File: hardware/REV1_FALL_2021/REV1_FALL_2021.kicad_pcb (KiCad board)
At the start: 2 copper layers, 146 x 133.4 mm, 40 parts, among them J101 Screw_Terminal_01x02, J102 Screw_Terminal_01x02, Q101 Q_NMOS_GDS, Q102 Q_NMOS_GDS, U1 Teensy3.6_All_Pins, U2 PA16165_Breakout, U201 TPS2113ADRBR, U3 MPL3115A2_Breakout, U301 TPS2113ADRBR, U4 BNO055_Breakout, U5 RFM69HCW_Breakout

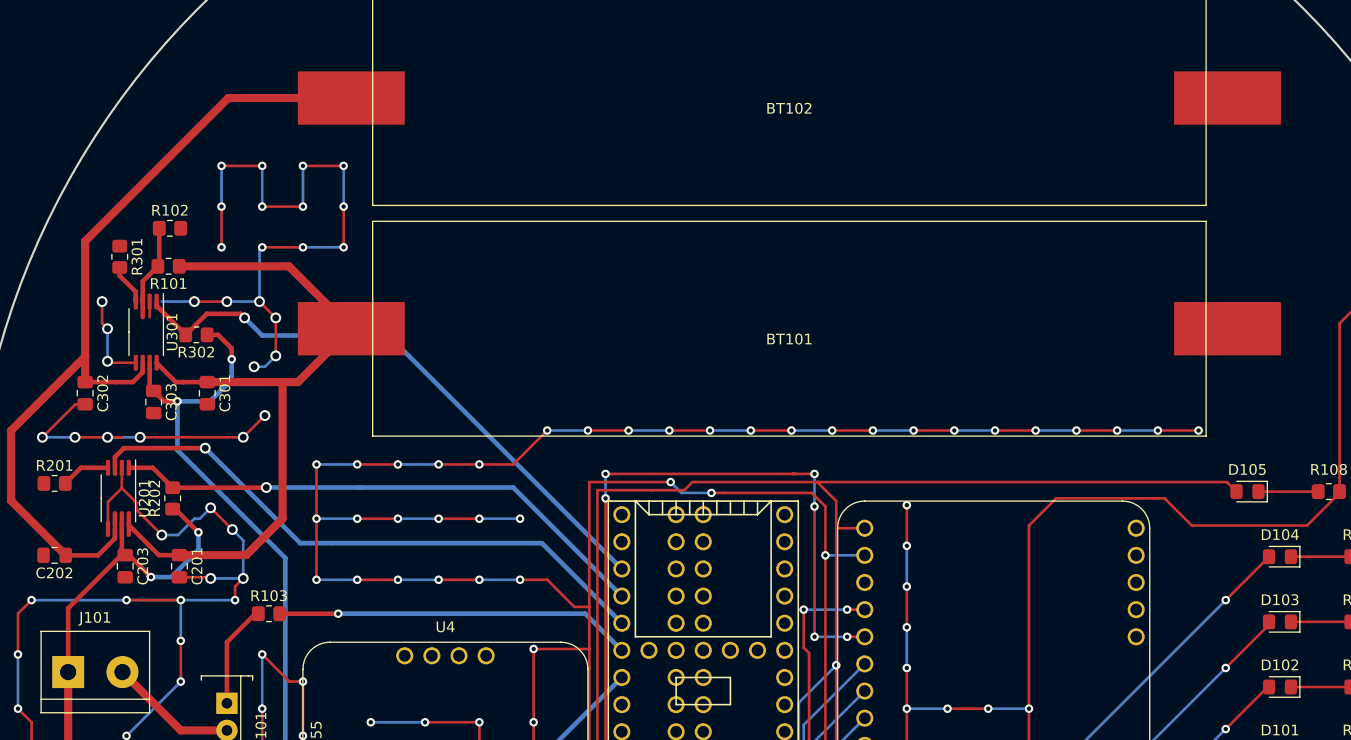
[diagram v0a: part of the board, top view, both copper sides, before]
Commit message: add dot to pin 1 of TPS2113A, rewire traces slightly
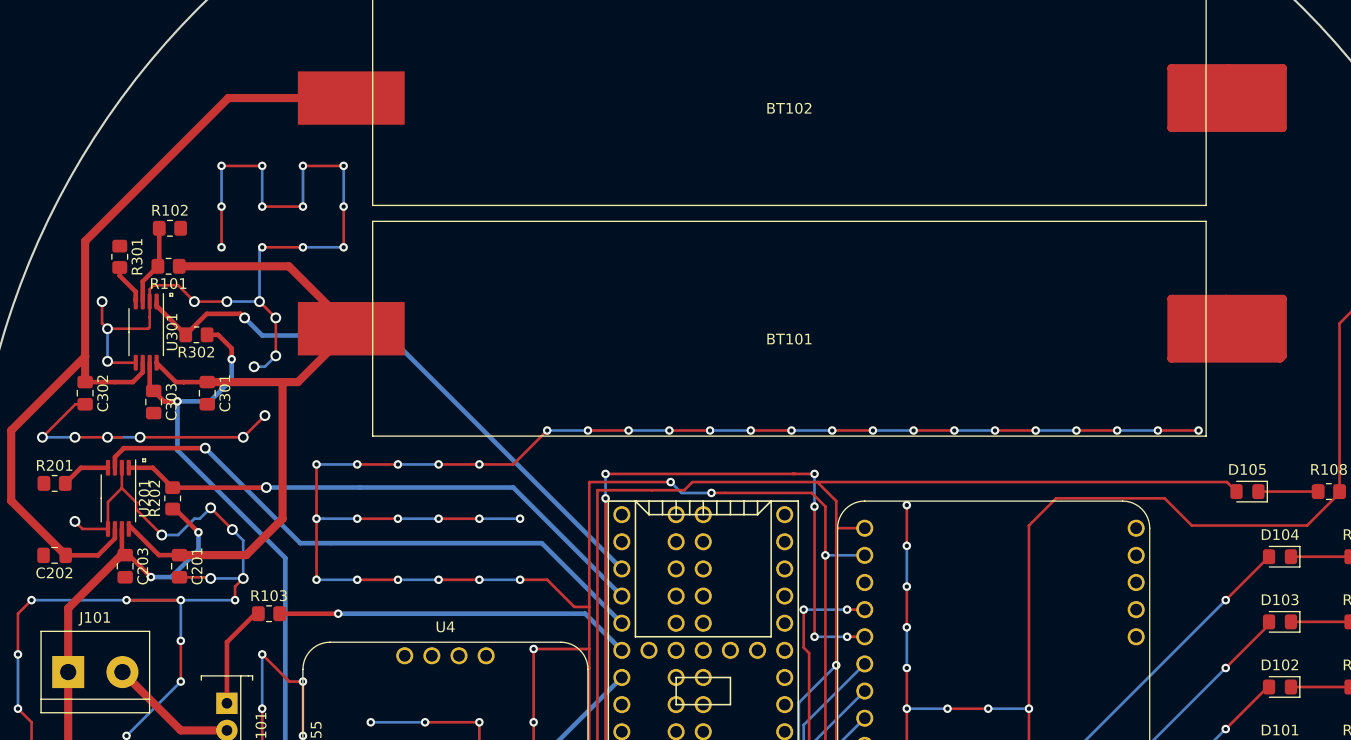
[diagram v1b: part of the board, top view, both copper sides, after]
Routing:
- net GND: track 996.9 -> 1075.0 mm, vias 176 -> 177
- net /V_EMATCH: track 63.3 -> 75.0 mm
- net /TPS2113A for Teensy power/VSNS: track 9.31 -> 7.49 mm
- net /TPS2113A for E-match/IN1: track 70.6 -> 69.5 mm
- net /TPS2113A for E-match/IN2: track 82.5 -> 81.4 mm
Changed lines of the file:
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@@
   (general
     (thickness 1.6)
-    (drawings 8)
-    (tracks 693)
+    (drawings 16)
+    (tracks 714)
     (zones 0)
     (modules 40)
@@
   )
   (setup
-    (last_trace_width 0.4318)
+    (last_trace_width 0.762)
     (user_trace_width 0.4318)
     (user_trace_width 0.762)
@@
     )
   )
+  (gr_line (start 43.688 93.726) (end 43.434 93.726) (angle 90) (layer F.SilkS) (width 0.12))
+  (gr_line (start 43.688 93.472) (end 43.688 93.726) (angle 90) (layer F.SilkS) (width 0.12))
+  (gr_line (start 43.434 93.472) (end 43.688 93.472) (angle 90) (layer F.SilkS) (width 0.12))
+  (gr_line (start 43.434 93.726) (end 43.434 93.472) (angle 90) (layer F.SilkS) (width 0.12))
+  (gr_line (start 46.228 77.978) (end 46.228 78.232) (angle 90) (layer F.SilkS) (width 0.12))
+  (gr_line (start 45.974 77.978) (end 46.228 77.978) (angle 90) (layer F.SilkS) (width 0.12))
+  (gr_line (start 45.974 78.232) (end 45.974 77.978) (angle 90) (layer F.SilkS) (width 0.12))
+  (gr_line (start 46.228 78.232) (end 45.974 78.232) (angle 90) (layer F.SilkS) (width 0.12))
   (gr_text - (at 134.62 45.72) (layer F.SilkS)
     (effects (font (size 3.81 3.81) (thickness 0.3)))
@@
   (segment (start 40.132 84.328) (end 40.132 81.28) (width 0.25) (layer B.Cu) (net 12))
   (via (at 40.132 84.328) (size 1.016) (drill 0.635) (layers F.Cu B.Cu) (net 12))
-  (segment (start 44.0765 80.1975) (end 44.0765 79.3675) (width 0.25) (layer F.Cu) (net 12) (status 400020))
+  (segment (start 44.0765 79.3675) (end 44.0765 80.1975) (width 0.25) (layer F.Cu) (net 12) (status 800020))
+  (segment (start 43.942 81.28) (end 40.132 81.28) (width 0.25) (layer F.Cu) (net 12))
+  (segment (start 44.0765 81.1455) (end 43.942 81.28) (width 0.25) (layer F.Cu) (net 12))
+  (segment (start 44.0765 80.1975) (end 44.0765 81.1455) (width 0.25) (layer F.Cu) (net 12))
   (via (at 53.848 84.836) (size 1.016) (drill 0.635) (layers F.Cu B.Cu) (net 12))
   (segment (start 54.864 84.836) (end 53.848 84.836) (width 0.25) (layer B.Cu) (net 12))
@@
   (via (at 55.88 83.82) (size 1.016) (drill 0.635) (layers F.Cu B.Cu) (net 12))
   (segment (start 55.88 80.264) (end 55.88 83.82) (width 0.25) (layer F.Cu) (net 12))
-  (segment (start 45.212 78.74) (end 48.26 78.74) (width 0.25) (layer B.Cu) (net 12))
   (via (at 48.26 78.74) (size 1.016) (drill 0.635) (layers F.Cu B.Cu) (net 12))
+  (segment (start 46.736 77.216) (end 48.26 78.74) (width 0.25) (layer F.Cu) (net 12))
+  (segment (start 44.45 77.216) (end 46.736 77.216) (width 0.25) (layer F.Cu) (net 12))
+  (segment (start 44.0765 77.5895) (end 44.45 77.216) (width 0.25) (layer F.Cu) (net 12))
+  (segment (start 44.0765 78.735) (end 44.0765 77.5895) (width 0.25) (layer F.Cu) (net 12) (status 400000))
+  (segment (start 51.308 78.74) (end 54.356 78.74) (width 0.25) (layer B.Cu) (net 12))
+  (via (at 51.308 78.74) (size 1.016) (drill 0.635) (layers F.Cu B.Cu) (net 12))
   (segment (start 48.26 78.74) (end 51.308 78.74) (width 0.25) (layer F.Cu) (net 12))
-  (via (at 51.308 78.74) (size 1.016) (drill 0.635) (layers F.Cu B.Cu) (net 12))
-  (segment (start 51.308 78.74) (end 54.356 78.74) (width 0.25) (layer B.Cu) (net 12))
   (via (at 54.356 78.74) (size 1.016) (drill 0.635) (layers F.Cu B.Cu) (net 12))
   (segment (start 54.356 78.74) (end 55.88 80.264) (width 0.25) (layer F.Cu) (net 12))
@@
   (segment (start 40.173 100.0175) (end 40.173 97.495) (width 0.25) (layer F.Cu) (net 12) (status 400000))
   (segment (start 40.173 97.495) (end 41.473 96.195) (width 0.25) (layer F.Cu) (net 12))
-  (segment (start 41.473 98.555) (end 41.473 101.854) (width 0.4318) (layer F.Cu) (net 13) (status 400000))
-  (segment (start 41.473 101.854) (end 41.473 102.1575) (width 0.4318) (layer F.Cu) (net 13) (status 800020))
+  (segment (start 145.034 56.896) (end 139.7 56.896) (width 0.762) (layer F.Cu) (net 12))
+  (segment (start 150.114 56.896) (end 145.034 56.896) (width 0.762) (layer F.Cu) (net 12))
+  (segment (start 150.114 62.484) (end 150.114 56.896) (width 0.762) (layer F.Cu) (net 12))
+  (segment (start 139.7 62.484) (end 150.114 62.484) (width 0.762) (layer F.Cu) (net 12))
+  (segment (start 139.7 56.896) (end 139.7 62.484) (width 0.762) (layer F.Cu) (net 12))
+  (segment (start 144.945 81.28) (end 144.945 78.575) (width 0.762) (layer F.Cu) (net 12) (status 400000))
+  (segment (start 150.114 78.486) (end 144.78 78.486) (width 0.762) (layer F.Cu) (net 12))
+  (segment (start 150.114 83.82) (end 150.114 78.486) (width 0.762) (layer F.Cu) (net 12))
+  (segment (start 139.7 78.486) (end 139.7 84.074) (width 0.762) (layer F.Cu) (net 12))
+  (segment (start 144.856 78.486) (end 139.7 78.486) (width 0.762) (layer F.Cu) (net 12))
+  (segment (start 144.945 78.575) (end 144.856 78.486) (width 0.762) (layer F.Cu) (net 12))
+  (segment (start 139.7 84.074) (end 149.86 84.074) (width 0.762) (layer F.Cu) (net 12))
+  (segment (start 149.86 84.074) (end 150.114 83.82) (width 0.762) (layer F.Cu) (net 12))
+  (segment (start 40.173 100.0175) (end 37.7875 100.0175) (width 0.25) (layer F.Cu) (net 12) (status 400000))
+  (via (at 37.084 99.314) (size 1.016) (drill 0.635) (layers F.Cu B.Cu) (net 12))
+  (segment (start 37.7875 100.0175) (end 37.084 99.314) (width 0.25) (layer F.Cu) (net 12))
   (segment (start 41.473 102.1575) (end 41.783 102.4675) (width 0.4318) (layer F.Cu) (net 13) (status C00030))
   (segment (start 41.783 102.4675) (end 42.1425 102.4675) (width 0.4318) (layer F.Cu) (net 13) (status C00030))
@@
   (via (at 44.196 104.521) (size 0.8) (drill 0.4) (layers F.Cu B.Cu) (net 13))
   (segment (start 42.1425 102.4675) (end 44.196 104.521) (width 0.4318) (layer F.Cu) (net 13) (status 400010))
-  (segment (start 41.473 101.854) (end 41.473 102.418) (width 0.4318) (layer F.Cu) (net 13) (status 800020))
   (segment (start 41.473 102.418) (end 36.449 107.442) (width 0.4318) (layer F.Cu) (net 13) (status 400010))
   (segment (start 36.449 107.442) (end 36.449 113.411) (width 0.4318) (layer F.Cu) (net 13) (status 800020))
@@
   (segment (start 43.561 127.635) (end 43.561 137.287) (width 0.762) (layer F.Cu) (net 13))
   (segment (start 36.449 120.523) (end 43.561 127.635) (width 0.762) (layer F.Cu) (net 13))
+  (segment (start 41.473 100.0175) (end 41.473 102.1575) (width 0.4318) (layer F.Cu) (net 13) (status C00000))
+  (segment (start 41.473 102.1575) (end 41.783 102.4675) (width 0.4318) (layer F.Cu) (net 13) (status C00000))
+  (segment (start 41.783 102.4675) (end 41.4235 102.4675) (width 0.762) (layer F.Cu) (net 13) (status C00000))
+  (segment (start 41.4235 102.4675) (end 36.449 107.442) (width 0.762) (layer F.Cu) (net 13) (status 400000))
+  (segment (start 36.449 107.442) (end 36.449 113.411) (width 0.762) (layer F.Cu) (net 13) (status 800000))
   (segment (start 50.4825 81.8515) (end 49.4505 81.8515) (width 0.4318) (layer F.Cu) (net 14) (status 800020))
   (segment (start 46.6725 88.0745) (end 49.7205 88.0745) (width 0.4318) (layer B.Cu) (net 14))
@@
   (segment (start 51.308 110.617) (end 51.308 116.332) (width 0.4318) (layer F.Cu) (net 16) (status 800020))
   (segment (start 53.975 107.95) (end 51.308 110.617) (width 0.4318) (layer F.Cu) (net 16) (status 400010))
-  (segment (start 43.4265 78.3825) (end 43.4265 80.1975) (width 0.4318) (layer F.Cu) (net 17) (status 800010))
   (segment (start 43.4265 78.735) (end 43.4265 76.8585) (width 0.4318) (layer F.Cu) (net 17) (status 400000))
   (segment (start 43.4265 76.8585) (end 44.974 75.311) (width 0.4318) (layer F.Cu) (net 17) (status 800000))
@@
   (segment (start 47.286 86.275) (end 47.244 86.275) (width 0.4318) (layer F.Cu) (net 23) (status 20))
   (segment (start 47.244 86.275) (end 49.4665 86.275) (width 0.4318) (layer F.Cu) (net 23) (status 800020))
-  (segment (start 42.123 98.555) (end 42.123 99.654) (width 0.4318) (layer F.Cu) (net 23) (status 400020))
   (segment (start 44.9365 102.4675) (end 46.863 102.4675) (width 0.4318) (layer F.Cu) (net 23) (status 800020))
   (segment (start 42.123 99.654) (end 44.9365 102.4675) (width 0.4318) (layer F.Cu) (net 23) (status 10))
@@
   (segment (start 42.503 86.275) (end 43.4265 85.3515) (width 0.4318) (layer F.Cu) (net 24))
   (segment (start 40.852 86.275) (end 42.503 86.275) (width 0.4318) (layer F.Cu) (net 24))
-  (segment (start 40.823 98.555) (end 40.823 99.639) (width 0.4318) (layer F.Cu) (net 24) (status 400020))
   (segment (start 64.215 59.69) (end 51.435 59.69) (width 0.762) (layer F.Cu) (net 24) (status 10))
   (segment (start 38.0365 73.0885) (end 38.0365 83.82) (width 0.762) (layer F.Cu) (net 24))

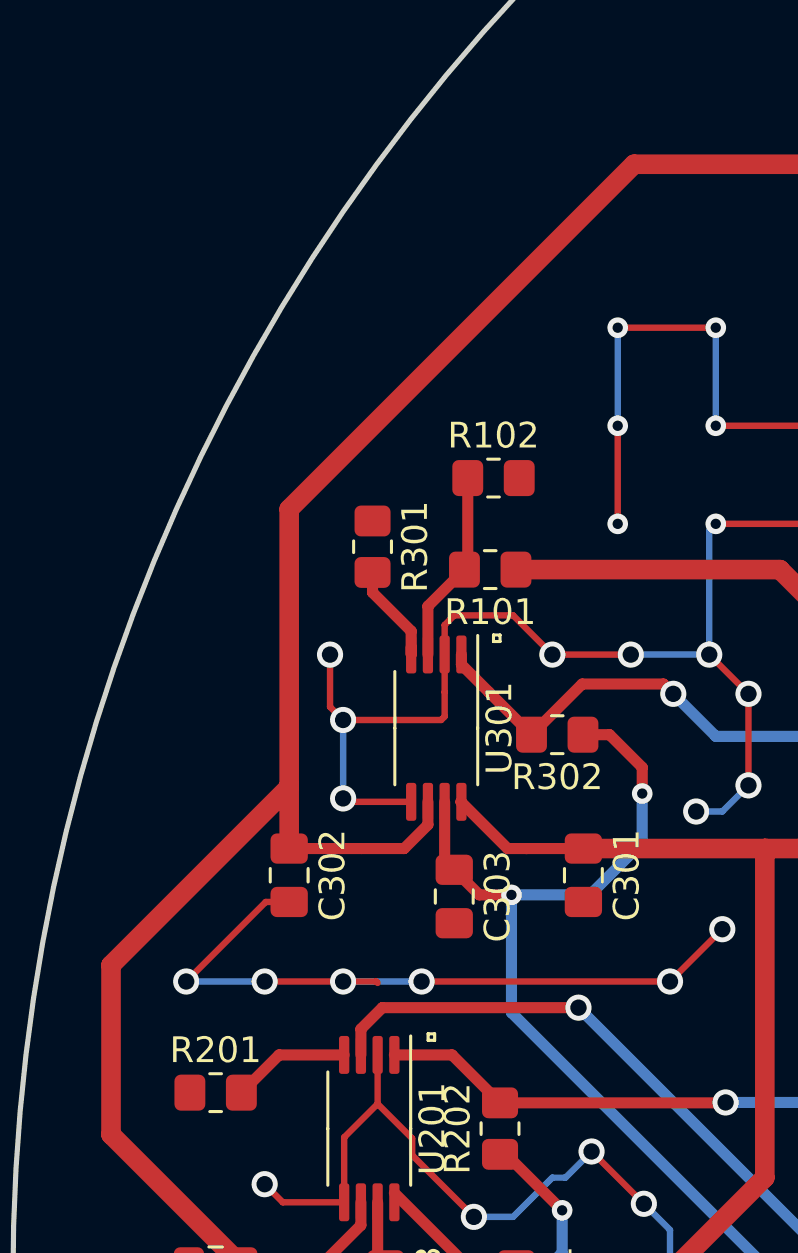
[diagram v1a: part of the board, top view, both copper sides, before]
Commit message: add series resistor to improve accuracy of ILIM resistor
It used to be a 400 ohm resistor, but those are not in stock in JLC's assembly parts. Now it is two 200 ohm resistors in series. It is important to get the values precise, because the maximum rating of the (inferior, but the only one in stock) TPS2113A is 1.25A, which is also the minimum all-fire current on the E-matches. So we need exactly 1.25A, not above, and not below.
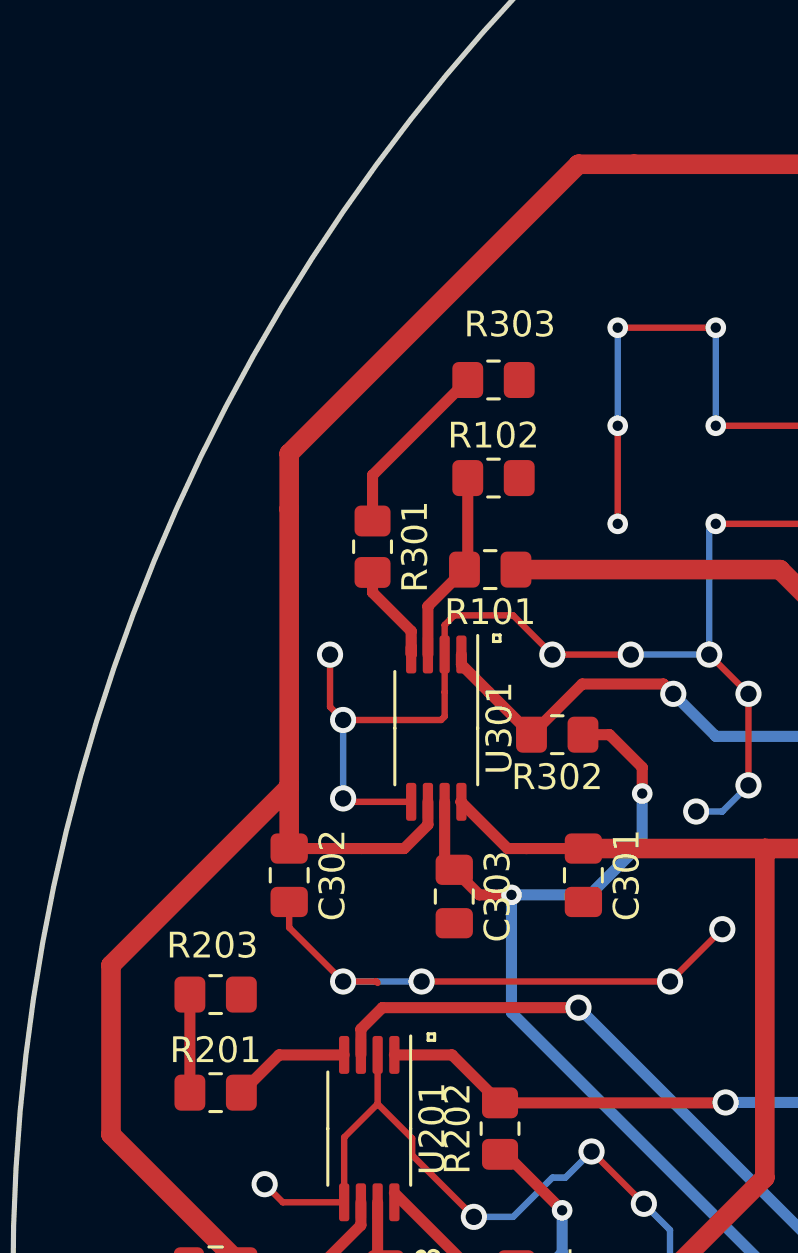
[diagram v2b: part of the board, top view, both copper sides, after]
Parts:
- removed G***: LOGO, Olin_Rocketry:Olin_O
- removed G***: LOGO, Olin_Rocketry:Olin_Rocketry_Logo1
- added R203: R_200, Resistor_SMD:R_0805_2012Metric_Pad1.20x1.40mm_HandSolder, F.Cu at (35.2, 91.9)
- added R303: R_200, Resistor_SMD:R_0805_2012Metric_Pad1.20x1.40mm_HandSolder, F.Cu at (46.0, 68.1)
- R201, R301: value R_270 -> R_200
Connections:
- R201 pad 1: GND -> Net-(R201-Pad1)
- R301 pad 1: GND -> Net-(R301-Pad1)
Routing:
- net GND: track 1075.0 -> 1067.6 mm, vias 177 -> 175
- net Net-(R301-Pad1): track 0.00 -> 7.01 mm
- net Net-(R201-Pad1): track 0.00 -> 3.81 mm
- net /TPS2113A for E-match/IN2: track 81.4 -> 82.6 mm

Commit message: update all fab-outputs, as ordered
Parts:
- added G***: LOGO, Olin_Rocketry:Olin_O, B.Cu at (100.3, 73.7)
- added G***: LOGO, Olin_Rocketry:Olin_Rocketry_Logo1, B.Cu at (100.3, 113.0)
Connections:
- U1 pad 16: (no net) -> Net-(U1-Pad16)
- U1 pad 17: (no net) -> Net-(U1-Pad17)
- U1 pad 18: (no net) -> Net-(U1-Pad18)
- U1 pad 19: (no net) -> Net-(U1-Pad19)
- U1 pad 20: (no net) -> Net-(U1-Pad20)
- U1 pad 21: (no net) -> Net-(U1-Pad21)
- U1 pad 22: (no net) -> Net-(U1-Pad22)
- U1 pad 23: (no net) -> Net-(U1-Pad23)
- U1 pad 24: (no net) -> Net-(U1-Pad24)
- U1 pad 25: (no net) -> Net-(U1-Pad25)
- U1 pad 26: (no net) -> Net-(U1-Pad26)
- U1 pad 27: (no net) -> Net-(U1-Pad27)
- U1 pad 28: (no net) -> Net-(U1-Pad28)
- U1 pad 29: (no net) -> Net-(U1-Pad29)
- U1 pad 30: (no net) -> Net-(U1-Pad30)
- U1 pad 31: (no net) -> Net-(U1-Pad31)
- U1 pad 37: (no net) -> Net-(U1-Pad37)
- U1 pad 38: (no net) -> Net-(U1-Pad38)
- U1 pad 41: (no net) -> Net-(U1-Pad41)
- U1 pad 42: (no net) -> Net-(U1-Pad42)
- U1 pad 43: (no net) -> Net-(U1-Pad43)
- U1 pad 44: (no net) -> Net-(U1-Pad44)
- U1 pad 47: (no net) -> Net-(U1-Pad47)
- U1 pad 48: (no net) -> Net-(U1-Pad48)
- U1 pad 49: (no net) -> Net-(U1-Pad49)
- U1 pad 50: (no net) -> Net-(U1-Pad50)
- U1 pad 52: (no net) -> Net-(U1-Pad52)
- U1 pad 54: (no net) -> Net-(U1-Pad54)
- U1 pad 55: (no net) -> Net-(U1-Pad55)
- U1 pad 56: (no net) -> Net-(U1-Pad56)
- U1 pad 57: (no net) -> Net-(U1-Pad57)
- U1 pad 58: (no net) -> Net-(U1-Pad58)
- U1 pad 59: (no net) -> Net-(U1-Pad59)
- U1 pad 6: (no net) -> Net-(U1-Pad6)
- U1 pad 60: (no net) -> Net-(U1-Pad60)
- U1 pad 61: (no net) -> Net-(U1-Pad61)
- U1 pad 62: (no net) -> Net-(U1-Pad62)
- U1 pad 63: (no net) -> Net-(U1-Pad63)
- U1 pad 64: (no net) -> Net-(U1-Pad64)
- U1 pad 65: (no net) -> Net-(U1-Pad65)
- U1 pad 66: (no net) -> Net-(U1-Pad66)
- U1 pad 67: (no net) -> Net-(U1-Pad67)
- U1 pad 68: (no net) -> Net-(U1-Pad68)
- U1 pad 69: (no net) -> Net-(U1-Pad69)
- U1 pad 7: (no net) -> Net-(U1-Pad7)
- U1 pad 70: (no net) -> Net-(U1-Pad70)
- U1 pad 71: (no net) -> Net-(U1-Pad71)
- U1 pad 72: (no net) -> Net-(U1-Pad72)
- U1 pad 73: (no net) -> Net-(U1-Pad73)
- U1 pad 74: (no net) -> Net-(U1-Pad74)
- U1 pad 75: (no net) -> Net-(U1-Pad75)
- U1 pad 76: (no net) -> Net-(U1-Pad76)
- U1 pad 77: (no net) -> Net-(U1-Pad77)
- U1 pad 78: (no net) -> Net-(U1-Pad78)
- U1 pad 79: (no net) -> Net-(U1-Pad79)
- U1 pad 80: (no net) -> Net-(U1-Pad80)
- U1 pad 81: (no net) -> Net-(U1-Pad81)
- U1 pad 82: (no net) -> Net-(U1-Pad82)
- U1 pad 83: (no net) -> Net-(U1-Pad83)
- U1 pad 84: (no net) -> Net-(U1-Pad84)
- U1 pad 85: (no net) -> Net-(U1-Pad85)
- U1 pad 86: (no net) -> Net-(U1-Pad86)
- U1 pad 87: (no net) -> Net-(U1-Pad87)
- U1 pad 88: (no net) -> Net-(U1-Pad88)
- U2 pad 1: (no net) -> Net-(U2-Pad1)
- U2 pad 2: (no net) -> Net-(U2-Pad2)
- U2 pad 3: (no net) -> Net-(U2-Pad3)
- U2 pad 4: (no net) -> Net-(U2-Pad4)
- U2 pad 9: (no net) -> Net-(U2-Pad9)
- U3 pad 3: (no net) -> Net-(U3-Pad3)
- U3 pad 4: (no net) -> Net-(U3-Pad4)
- U3 pad 5: (no net) -> Net-(U3-Pad5)
- U4 pad 10: (no net) -> Net-(U4-Pad10)
- U4 pad 2: (no net) -> Net-(U4-Pad2)
- U4 pad 6: (no net) -> Net-(U4-Pad6)
- U4 pad 7: (no net) -> Net-(U4-Pad7)
- U4 pad 8: (no net) -> Net-(U4-Pad8)
- U4 pad 9: (no net) -> Net-(U4-Pad9)
- U5 pad 10: (no net) -> Net-(U5-Pad10)
- U5 pad 11: (no net) -> Net-(U5-Pad11)
- U5 pad 12: (no net) -> Net-(U5-Pad12)
- U5 pad 13: (no net) -> Net-(U5-Pad13)
- U5 pad 14: (no net) -> Net-(U5-Pad14)
- U5 pad 3: (no net) -> Net-(U5-Pad3)
